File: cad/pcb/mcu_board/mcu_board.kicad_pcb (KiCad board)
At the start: 2 copper layers, 20 x 52 mm, 28 parts, among them J1 Pin header, J2 EMI Shield, J3 FFC8, J4 Display interface, Q1 BC847C, U1 MCP6001T-I/OT, U2 STM32F103CBTx, U3 NCP1117-3.3_SOT223, Y1 XC32M4-8.000 12pF

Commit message: Change: Update uC PCB
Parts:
- removed G***: LOGO, Icons_Graphics:retronics_logo_14mm
- added C11: 10µF, Capacitor_SMD:C_1206_3216Metric_Pad1.33x1.80mm_HandSolder, F.Cu at (144.8, 88.1)
- added R10: 0, Resistor_SMD:R_0603_1608Metric_Pad0.98x0.95mm_HandSolder, F.Cu at (154.6, 62.2)
- added R11: 0, Resistor_SMD:R_0603_1608Metric_Pad0.98x0.95mm_HandSolder, F.Cu at (153.1, 62.2)
- added R12: 0, Resistor_SMD:R_0603_1608Metric_Pad0.98x0.95mm_HandSolder, F.Cu at (151.6, 62.2)
- added R13: 0, Resistor_SMD:R_0603_1608Metric_Pad0.98x0.95mm_HandSolder, F.Cu at (150.1, 62.2)
- added R8: 2k7, Resistor_SMD:R_0603_1608Metric_Pad0.98x0.95mm_HandSolder, F.Cu at (154.8, 89.5)
- added R9: 4k7, Resistor_SMD:R_0603_1608Metric_Pad0.98x0.95mm_HandSolder, F.Cu at (154.8, 86.0)
- C2: footprint Capacitor_SMD:C_0603_1608Metric_Pad1.08x0.95mm_HandSolder -> Capacitor_SMD:C_1206_3216Metric_Pad1.33x1.80mm_HandSolder
- C4, C5: footprint Retronics_Passives:C_0603_1608Metric_Pad1.08x0.95mm_HandSolder -> Capacitor_SMD:C_1206_3216Metric_Pad1.33x1.80mm_HandSolder
- J1: value Pin header -> Pin Header; footprint Retronics_Connectors:PinHeader_1x03_P2.54mm_Horizontal_Alt -> Connector_PinHeader_2.54mm:PinHeader_1x05_P2.54mm_Horizontal
- J3: footprint myDevices:0527450897 -> Connector_PinHeader_2.54mm:PinHeader_1x08_P2.54mm_Vertical_SMD_Pin1Left
- R7: moved to F.Cu
- U2: value STM32F103CBTx -> STM32F303CBTx
- U3: value NCP1117-3.3_SOT223 -> NCP1117-Adj_SOT223
- moved R4 9.97 mm to (143.4, 74.8), turned to 180 degrees
- moved J1 2.98 mm to (145.0, 97.0)
- moved J3 1.12 mm to (150.0, 54.6), turned to 90 degrees
- moved C4 1.00 mm to (157.7, 84.5)
- moved C2 0.74 mm to (143.6, 77.3)
- moved C5 0.48 mm to (149.8, 84.2), turned to 0 degrees
- moved R7 0.15 mm to (141.8, 87.6)
- moved C8 0.08 mm to (149.8, 65.1)
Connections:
- J1 pad 1: Net-(J1-Pin_1) -> unconnected-(J1-Pin_1-Pad1)
- J1 pad 2: GND -> Net-(J1-Pin_2)
- J1 pad 3: /AGC -> GND
- U2 pad 21: unconnected-(U2-PB10_SCL2_TX3-Pad21) -> EN
- U2 pad 39: unconnected-(U2-PB3_SCK1-Pad39) -> Net-(U2-PB3_SCK1)
- U2 pad 40: unconnected-(U2-PB4_MISO1-Pad40) -> Net-(U2-PB4_MISO1)
- U2 pad 41: unconnected-(U2-PB5_MOSI1-Pad41) -> Net-(U2-PB5_MOSI1)
- U2 pad 42: unconnected-(U2-PB6_TX1_SCL1_PWM-Pad42) -> Net-(U2-PB6_TX1_SCL1_PWM)
- U3 pad 1: GND -> Net-(U3-GND)
- U3 pad 3: Net-(J1-Pin_1) -> Net-(J1-Pin_2)
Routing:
- net +3.3V: track 59.0 -> 85.9 mm, vias 4 -> 2
- net EN: track 0.00 -> 24.5 mm
- net GND: track 20.9 -> 39.7 mm, vias 25 -> 30
- net Net-(J1-Pin_2): track 0.00 -> 17.1 mm
- net Net-(J1-Pin_1): track 11.8 -> 0.00 mm, vias 1 -> 0
- net TX2: track 20.3 -> 29.2 mm
- net ~{RESET}: track 32.4 -> 39.2 mm, vias 2 -> 0
- net Net-(U2-PB6_TX1_SCL1_PWM): track 0.00 -> 5.85 mm
- net Net-(U2-PB5_MOSI1): track 0.00 -> 4.90 mm
- net Net-(U2-PB4_MISO1): track 0.00 -> 4.48 mm
- net RX2: track 19.7 -> 24.1 mm
- net Net-(U3-GND): track 0.00 -> 4.42 mm
- net DISP_BLK: track 17.5 -> 21.5 mm, vias 1 -> 2
- net Net-(U2-PB3_SCK1): track 0.00 -> 3.97 mm
- net SWDIO: track 19.9 -> 16.4 mm
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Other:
- board size 20 x 52 mm -> 20 x 50 mm
- board text added: "EM84 MCU Board DL2WAG Martin Wagner"
- board text added: "EN AGC GND VCC"
- board text removed: "6U5 MCU Board R0180B_2437 Bjørner Sandom"
- board text removed: "AGC GND VCC"

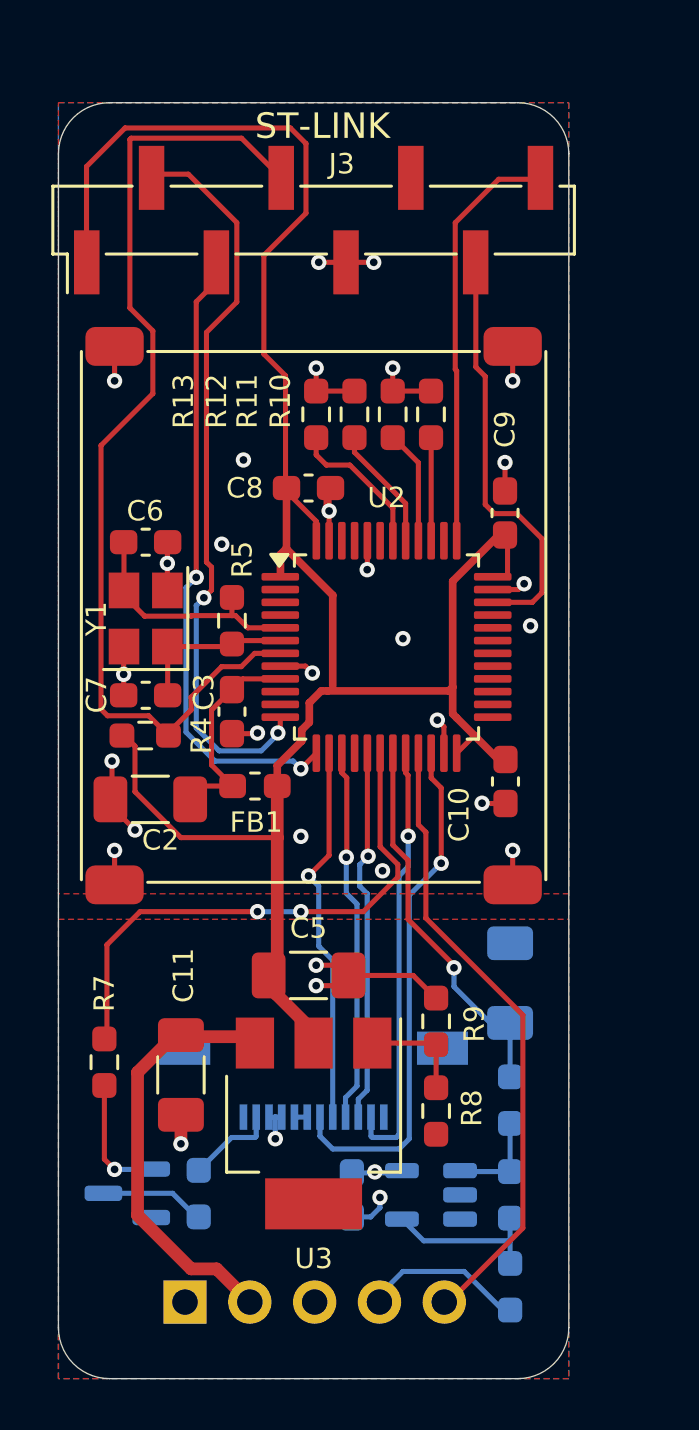
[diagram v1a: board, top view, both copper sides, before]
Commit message: Change: Add Jtag, Cleanup
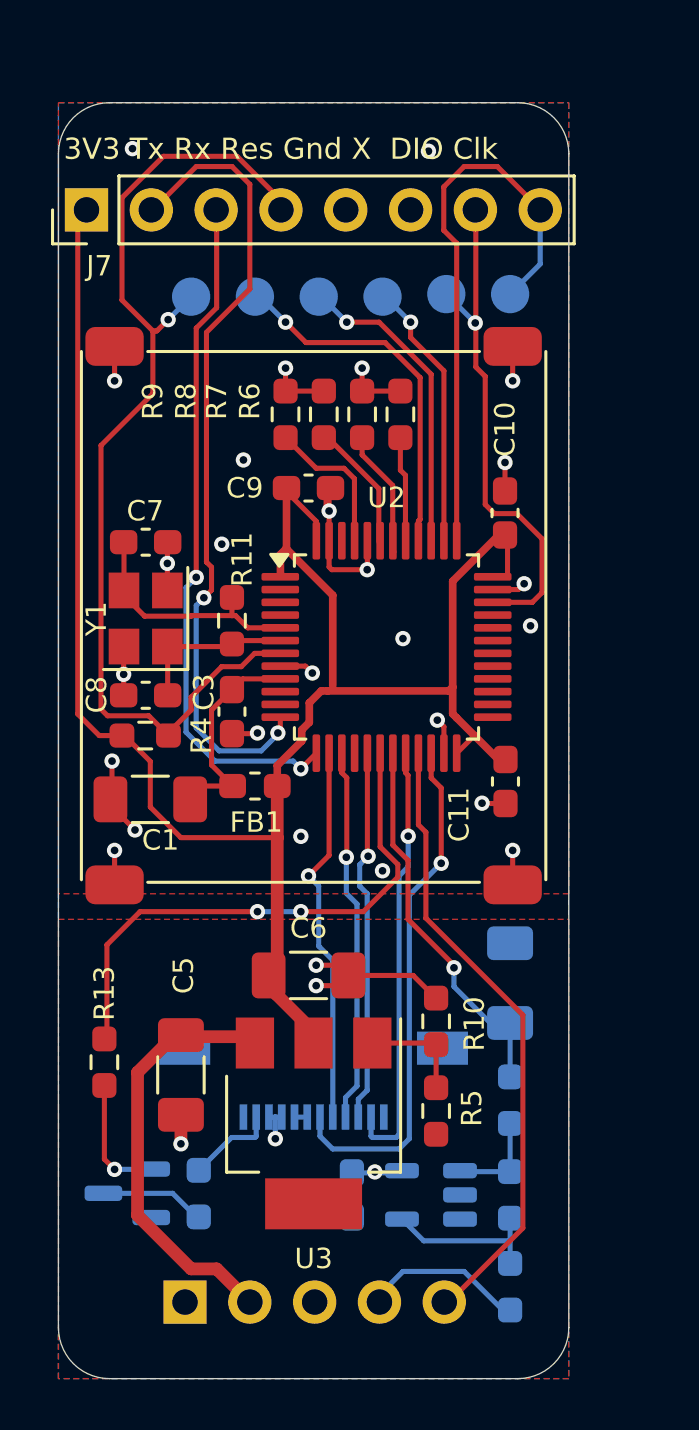
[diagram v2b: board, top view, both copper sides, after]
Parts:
- added J10: Conn_01x01_Pin, TestPoint:TestPoint_Pad_D1.5mm, B.Cu at (145.2, 57.6)
- added J3: Conn_01x01_Pin, TestPoint:TestPoint_Pad_D1.5mm, B.Cu at (155.2, 57.5)
- added J4: Conn_01x01_Pin, TestPoint:TestPoint_Pad_D1.5mm, B.Cu at (157.7, 57.5)
- added J6: Conn_01x01_Pin, TestPoint:TestPoint_Pad_D1.5mm, B.Cu at (152.7, 57.6)
- added J8: Conn_01x01_Pin, TestPoint:TestPoint_Pad_D1.5mm, B.Cu at (150.2, 57.6)
- added J9: Conn_01x01_Pin, TestPoint:TestPoint_Pad_D1.5mm, B.Cu at (147.7, 57.6)
- J7: renamed from J3; footprint Connector_PinHeader_2.54mm:PinHeader_1x08_P2.54mm_Vertical_SMD_Pin1Left -> Connector_PinHeader_2.54mm:PinHeader_1x08_P2.54mm_Vertical
- moved J7 8.91 mm to (141.1, 54.2)
- moved R6 1.20 mm to (153.4, 62.2)
- moved R7 1.20 mm to (151.9, 62.2)
- moved R8 1.20 mm to (150.4, 62.2)
- moved R9 1.20 mm to (148.9, 62.2)
- renumbered C2 to C1, C9 to C10, C10 to C11, C1 to C2, C11 to C5, C5 to C6, C6 to C7, C7 to C8, C8 to C9, J4 to J5, R9 to R10, R5 to R11, R6 to R12, R7 to R13, R8 to R5, R10 to R6, R11 to R7, R12 to R8, R13 to R9
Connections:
- R6 pad 1: Net-(U2-PB3_SCK1) -> Net-(U2-PB5_MOSI1)
- R7 pad 1: Net-(U2-PB4_MISO1) -> Net-(U2-PB6_TX1_SCL1_PWM)
- R8 pad 1: Net-(U2-PB5_MOSI1) -> Net-(U2-PB7_RX1_SDA1_PWM)
- R9 pad 1: Net-(U2-PB6_TX1_SCL1_PWM) -> Net-(U2-PB8_SCL1_PWM)
- U2 pad 38: unconnected-(U2-PA15-Pad38) -> JTDI
- U2 pad 39: Net-(U2-PB3_SCK1) -> JTDO
- U2 pad 40: Net-(U2-PB4_MISO1) -> JNTRST
- U2 pad 43: unconnected-(U2-PB7_RX1_SDA1_PWM-Pad43) -> Net-(U2-PB7_RX1_SDA1_PWM)
- U2 pad 45: unconnected-(U2-PB8_SCL1_PWM-Pad45) -> Net-(U2-PB8_SCL1_PWM)
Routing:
- net JNTRST: track 0.00 -> 14.2 mm, vias 0 -> 1
- net JTDO: track 0.00 -> 12.2 mm, vias 0 -> 1
- net JTDI: track 0.00 -> 10.6 mm, vias 0 -> 1
- net SWCLK: track 16.6 -> 22.7 mm
- net Net-(U2-PB8_SCL1_PWM): track 0.00 -> 5.77 mm
- net +3.3V: track 85.9 -> 80.3 mm
- net Net-(U2-PB7_RX1_SDA1_PWM): track 0.00 -> 5.06 mm
- net Net-(U2-PB4_MISO1): track 4.48 -> 0.00 mm
- net Net-(U2-PB3_SCK1): track 3.97 -> 0.00 mm
- net SWDIO: track 16.4 -> 19.9 mm, vias 0 -> 1
- net TX2: track 29.2 -> 31.8 mm
- net RX2: track 24.1 -> 26.7 mm
- net ~{RESET}: track 39.2 -> 40.6 mm, vias 0 -> 1
- net GND: track 39.7 -> 38.4 mm, vias 30 -> 29
- net Net-(U2-PB6_TX1_SCL1_PWM): track 5.85 -> 5.00 mm
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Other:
- board text added: "3V3 Tx Rx Res Gnd X DIO Clk"
- board text added: "Clk DIO X Gnd Res Rx Tx 3V3"
- board text added: "JTCK JTDO RES"
- board text added: "JTMS JTDI JNTRST"
- board text removed: "ST-LINK"
